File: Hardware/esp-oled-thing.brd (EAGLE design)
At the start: 48.3 x 27 mm, 44 parts, among them Q1 2.5A/30V, U1 MCP73831, U2 TPS61200

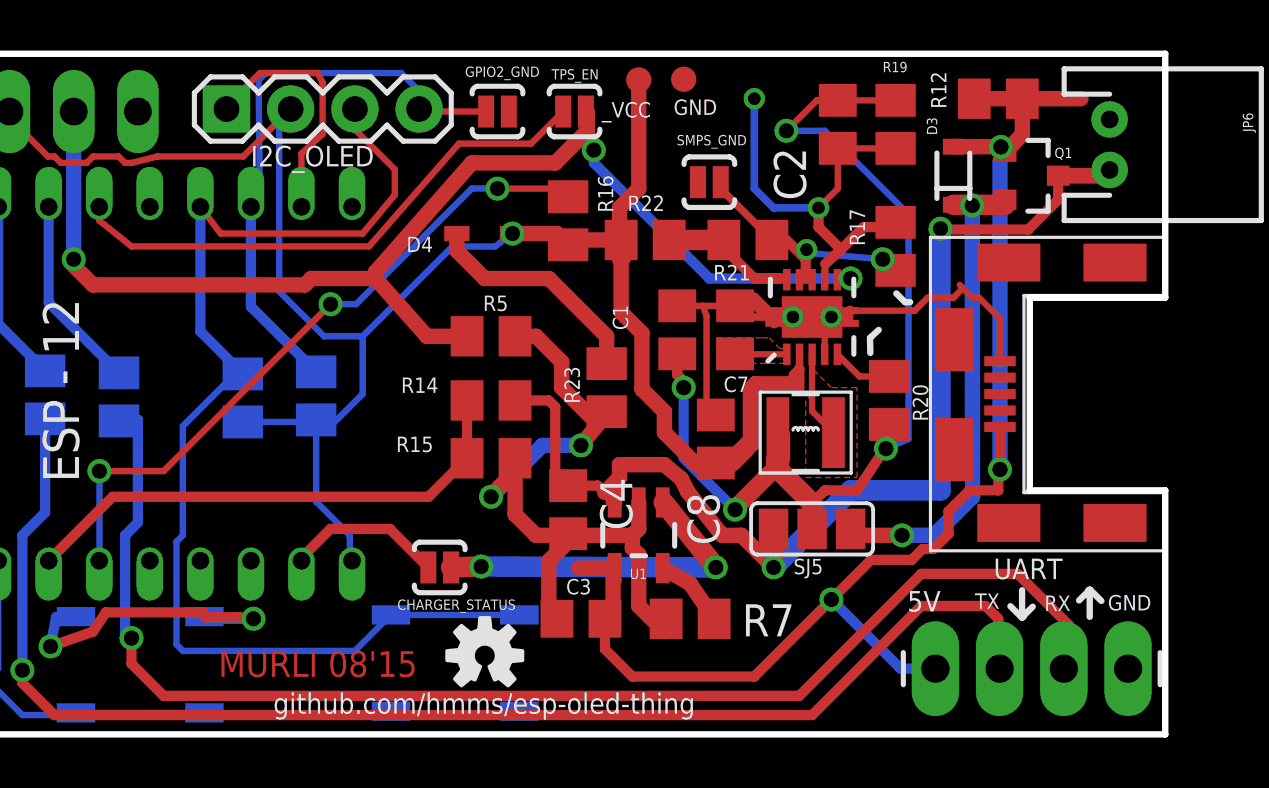
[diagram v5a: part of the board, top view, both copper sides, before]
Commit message: final DRC before sending it out. some errors fixed.
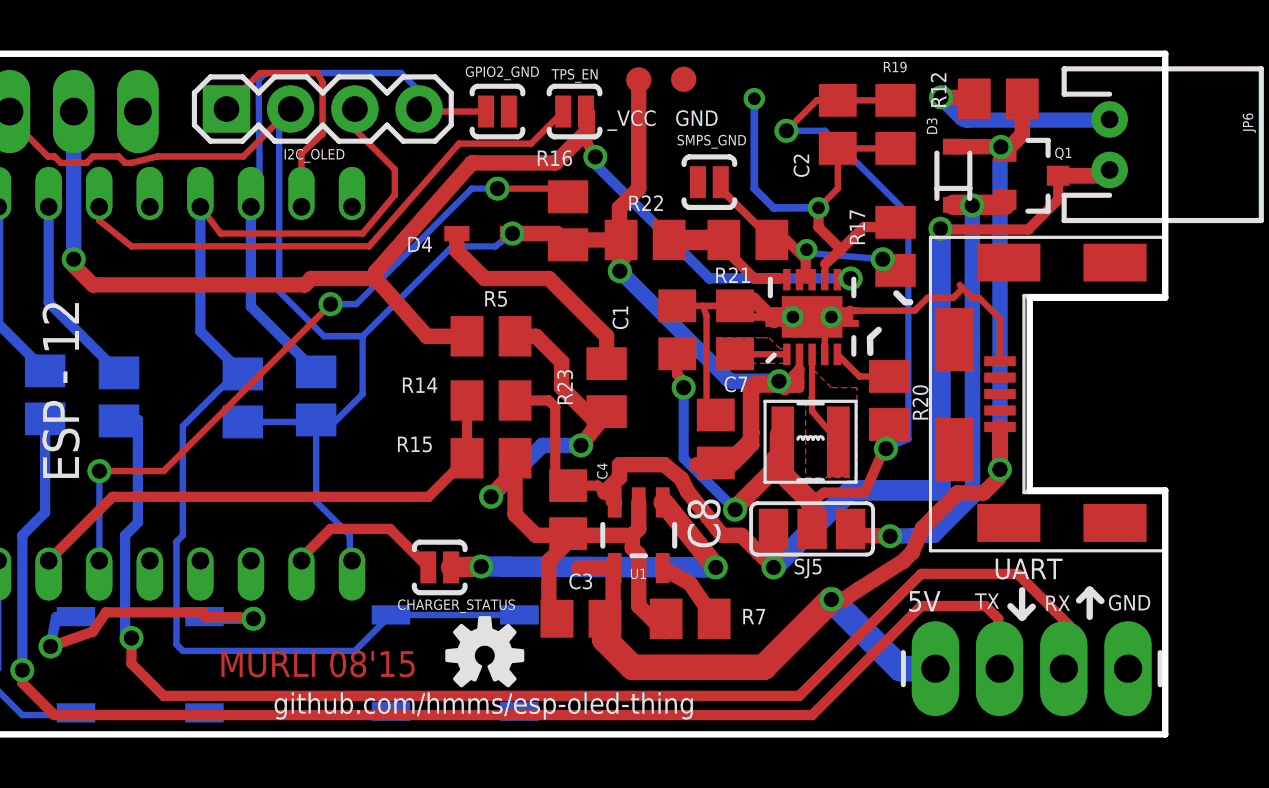
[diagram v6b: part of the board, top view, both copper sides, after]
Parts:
- moved U$3 0.41 mm to (34.2, 11.6)
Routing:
- net GND: track 81.8 -> 85.9 mm, vias 6 -> 7
- net 5VIN: track 49.7 -> 48.4 mm
- net VCC: track 85.7 -> 85.2 mm, vias 1 -> 3

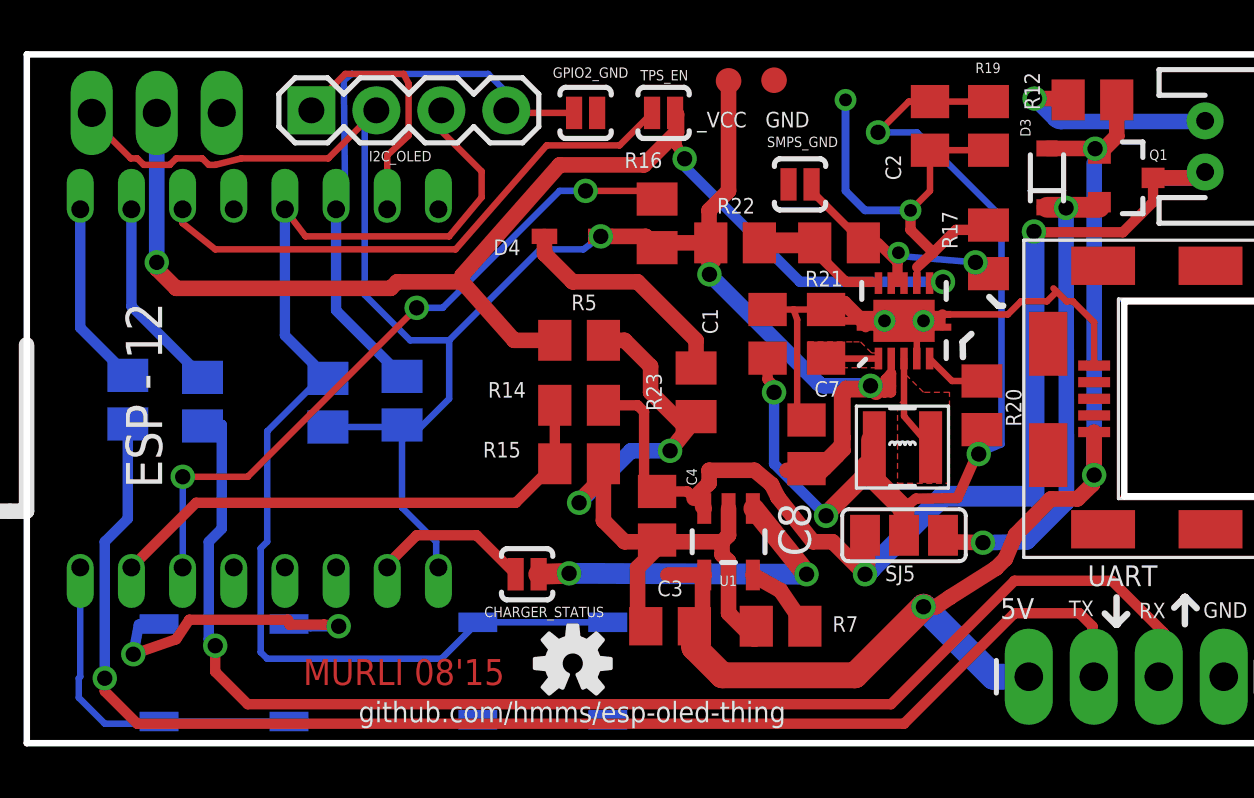
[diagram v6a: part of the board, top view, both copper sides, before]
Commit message: 'rev 2' hardware files sent to OSHPARK. NOT a final release, next release scheduled for end September with bug fixes - if any and aesthetic changes to fit in an enclosure.
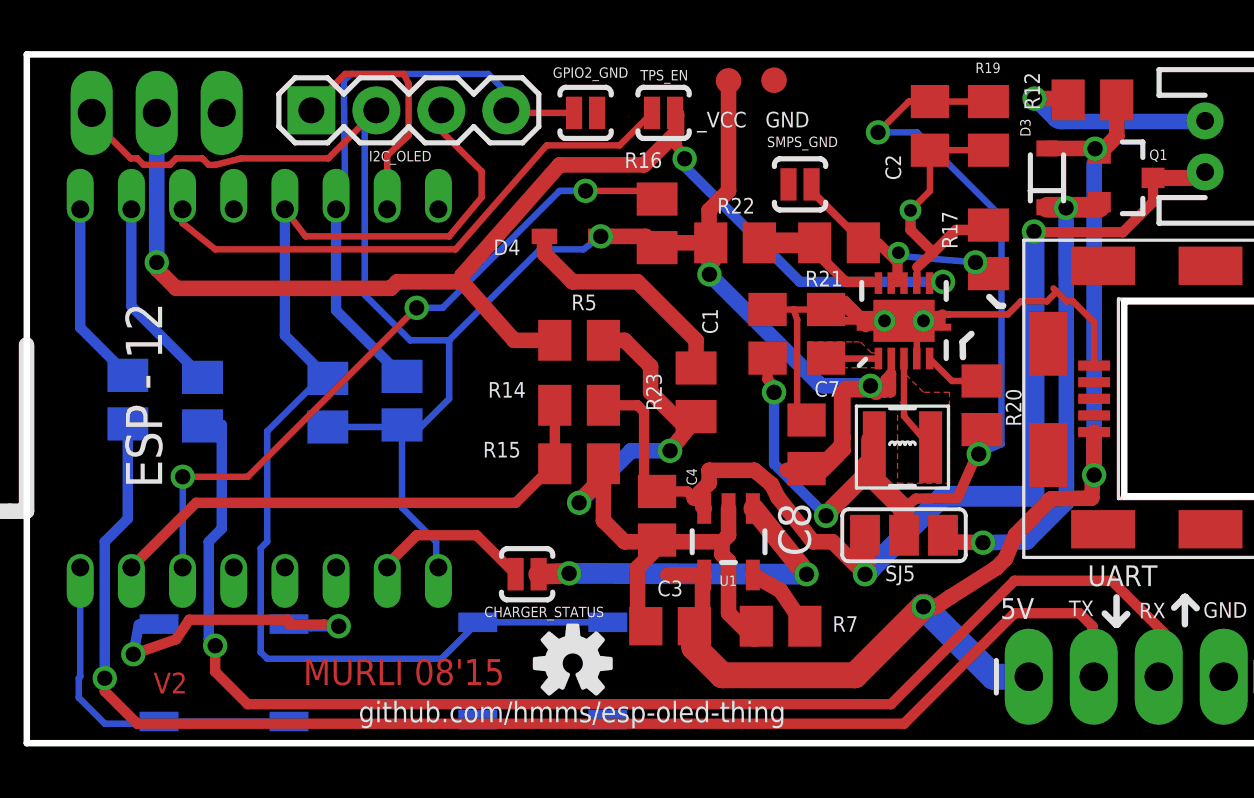
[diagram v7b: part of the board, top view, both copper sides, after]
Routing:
- net UVLO: track 17.5 -> 11.1 mm, vias 2 -> 1
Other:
- board text added: "V2"
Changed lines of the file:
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@@
 <wire x1="45.20945625" y1="5.6743625" x2="45.20945625" y2="5.65658125" width="0.254" layer="121"/>
 <wire x1="45.20945625" y1="5.65658125" x2="44.85131875" y2="5.29844375" width="0.254" layer="121"/>
+<text x="4.953" y="1.9431" size="0.8128" layer="1" font="vector">V2</text>
 </plain>
 <attributes>
@@
 </element>
 <element name="R1" library="adafruit" package="M0805" value="4.7K" x="11.77" y="13.31" locked="yes" smashed="yes" rot="MR270">
-<attribute name="NAME" x="10.474" y="16.654" size="1.27" layer="26" rot="MR180"/>
-<attribute name="VALUE" x="12.844" y="12.174" size="0.8128" layer="28" rot="MR90"/>
+<attribute name="NAME" x="10.36478125" y="10.9644" size="1.27" layer="26" rot="MR180"/>
+<attribute name="VALUE" x="11.043140625" y="15.630940625" size="0.8128" layer="28" rot="MR90"/>
 </element>
 <element name="R2" library="adafruit" package="M0805" value="4.7K" x="14.67" y="13.39" locked="yes" smashed="yes" rot="MR270">
-<attribute name="NAME" x="13.494" y="16.754" size="1.27" layer="26" rot="MR180"/>
-<attribute name="VALUE" x="16.856" y="14.506" size="0.8128" layer="28" rot="MR270"/>
+<attribute name="NAME" x="13.841978125" y="11.039" size="1.27" layer="26" rot="MR180"/>
+<attribute name="VALUE" x="13.5579625" y="15.51171875" size="0.8128" layer="28" rot="MR90"/>
 </element>
 <element name="U$2" library="esp8266modules" package="ESP12" value="ESP12" x="7.89" y="13.97" locked="yes" smashed="yes" rot="R90">
@@
 <element name="RST" library="SparkFun" package="TACTILE_SWITCH_SMD" value="" x="7.70968125" y="2.752859375" rot="MR0"/>
 <element name="R3" library="adafruit" package="M0805" value="100E" x="3.95" y="13.43" locked="yes" smashed="yes" rot="MR270">
-<attribute name="NAME" x="2.754" y="16.534" size="1.27" layer="26" rot="MR180"/>
-<attribute name="VALUE" x="2.936" y="14.646" size="0.8128" layer="28" rot="MR270"/>
+<attribute name="NAME" x="3.3059375" y="15.57338125" size="1.27" layer="26" rot="MR90"/>
+<attribute name="VALUE" x="2.76581875" y="14.463121875" size="0.8128" layer="28" rot="MR270"/>
 </element>
 <element name="R4" library="adafruit" package="M0805" value="100E" x="6.87" y="13.35" locked="yes" smashed="yes" rot="MR270">
-<attribute name="NAME" x="5.634" y="16.654" size="1.27" layer="26" rot="MR180"/>
-<attribute name="VALUE" x="5.856" y="14.566" size="0.8128" layer="28" rot="MR270"/>
+<attribute name="NAME" x="6.426978125" y="15.583178125" size="1.27" layer="26" rot="MR90"/>
+<attribute name="VALUE" x="9.191021875" y="14.733640625" size="0.8128" layer="28" rot="MR270"/>
 </element>
 <element name="I2C_OLED" library="SparkFun" package="1X04" value="" x="11.124" y="24.738" smashed="yes">
@@
 <wire x1="32.3723" y1="2.6543" x2="35.052" y2="5.334" width="1.016" layer="1"/>
 <wire x1="41.656" y1="10.414" x2="41.656" y2="10.11681875" width="0.6096" layer="1"/>
-<wire x1="41.656" y1="10.11681875" x2="41.0718" y2="9.5504" width="0.6096" layer="1"/>
-<wire x1="41.0718" y1="9.5504" x2="40.035478125" y2="9.5504" width="0.6096" layer="1"/>
+<wire x1="41.656" y1="10.11681875" x2="41.628059375" y2="9.58088125" width="0.6096" layer="1"/>
+<wire x1="41.628059375" y1="9.58088125" x2="40.035478125" y2="9.5504" width="0.6096" layer="1"/>
 <wire x1="41.722" y1="12.162" x2="41.722" y2="10.48" width="0.6096" layer="1"/>
 <wire x1="42.606" y1="23.728" x2="42.606" y2="25.146" width="0.6096" layer="1"/>
@@
 <wire x1="34.798" y1="18.034" x2="34.798" y2="17.993" width="0.254" layer="1"/>
 <wire x1="34.798" y1="17.993" x2="34.79" y2="17.985" width="0.254" layer="1"/>
-<via x="32.004" y="25.146" extent="1-16" drill="0.5"/>
-<wire x1="32.004" y1="21.59" x2="32.004" y2="25.146" width="0.3048" layer="16"/>
-<wire x1="32.004" y1="21.59" x2="32.766" y2="20.828" width="0.3048" layer="16"/>
-<wire x1="32.766" y1="20.828" x2="34.544" y2="20.828" width="0.3048" layer="16"/>
 <via x="34.544" y="20.828" extent="1-16" drill="0.5"/>
 <contactref element="C2" pad="2"/>

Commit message: parts ordered from Digikey,BOM added. Change quantity before ordering.
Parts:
- C1: value 10uF -> 10uF 10V
- C2, C7: value 0.1uF -> 0.1uF 10V
- C3, C4: value 4.7uF -> 4.7uF 10V
- C8: value 22uF -> 22uF 10V
- Q1: value 2.5A/30V -> DMP1045U
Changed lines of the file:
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@@
 <attribute name="VALUE" x="40.706040625" y="23.59151875" size="0.4064" layer="27" rot="R270"/>
 </element>
-<element name="Q1" library="SparkFun-DiscreteSemi" package="SOT23-3" value="2.5A/30V" x="42.926" y="22.098" smashed="yes" rot="R270">
+<element name="Q1" library="SparkFun-DiscreteSemi" package="SOT23-3" value="DMP1045U" x="42.926" y="22.098" smashed="yes" rot="R270">
 <attribute name="PROD_ID" value="TRANS-11308" x="50.546" y="34.798" size="1.778" layer="27" rot="R270" display="off"/>
 <attribute name="VALUE" value="2.5A/30V" x="50.546" y="34.798" size="1.778" layer="27" rot="R270" display="off"/>
@@
 <attribute name="VALUE" x="28.829" y="25.40761875" size="0.0254" layer="27"/>
 </element>
-<element name="C1" library="rcl" package="C0805" value="10uF" x="28.956" y="16.002" smashed="yes" rot="R90">
+<element name="C1" library="rcl" package="C0805" value="10uF 10V" x="28.956" y="16.002" smashed="yes" rot="R90">
 <attribute name="NAME" x="27.01544375" y="15.9893" size="0.6096" layer="25" rot="R90"/>
 <attribute name="VALUE" x="27.26435625" y="17.274534375" size="0.6096" layer="27" rot="R270"/>
 </element>
-<element name="C2" library="rcl" package="C0805" value="0.1uF" x="35.306" y="24.13" smashed="yes" rot="R270">
+<element name="C2" library="rcl" package="C0805" value="0.1uF 10V" x="35.306" y="24.13" smashed="yes" rot="R270">
 <attribute name="NAME" x="33.5661" y="23.0124" size="0.6096" layer="25" rot="R270"/>
 <attribute name="VALUE" x="36.357559375" y="22.0218" size="0.6096" layer="27" rot="R180"/>
 </element>
-<element name="C7" library="rcl" package="C0805" value="0.1uF" x="31.242" y="16.002" smashed="yes" rot="R90">
+<element name="C7" library="rcl" package="C0805" value="0.1uF 10V" x="31.242" y="16.002" smashed="yes" rot="R90">
 <attribute name="NAME" x="31.790640625" y="14.152878125" size="0.6096" layer="25" rot="R180"/>
 <attribute name="VALUE" x="30.28695625" y="15.483840625" size="0.4064" layer="27" rot="R90"/>
 </element>
-<element name="C8" library="rcl" package="C0805" value="22uF" x="30.48" y="11.684" smashed="yes" rot="R90">
+<element name="C8" library="rcl" package="C0805" value="22uF 10V" x="30.48" y="11.684" smashed="yes" rot="R90">
 <attribute name="NAME" x="30.65018125" y="7.30758125" size="1.27" layer="25" rot="R90"/>
 <attribute name="VALUE" x="32.115759375" y="10.767059375" size="0.6096" layer="27" rot="R90"/>
@@
 <attribute name="VALUE" x="29.16428125" y="2.8473375" size="0.6096" layer="27"/>
 </element>
-<element name="C3" library="rcl" package="C0805" value="4.7uF" x="25.146" y="4.572" smashed="yes" rot="R180">
+<element name="C3" library="rcl" package="C0805" value="4.7uF 10V" x="25.146" y="4.572" smashed="yes" rot="R180">
 <attribute name="NAME" x="25.648915625" y="6.355078125" size="0.6096" layer="25" rot="R180"/>
 <attribute name="VALUE" x="26.2763" y="3.44931875" size="0.6096" layer="27" rot="R180"/>
 </element>
-<element name="C4" library="rcl" package="C0805" value="4.7uF" x="24.638" y="8.89" smashed="yes" rot="R270">
+<element name="C4" library="rcl" package="C0805" value="4.7uF 10V" x="24.638" y="8.89" smashed="yes" rot="R270">
 <attribute name="NAME" x="25.78861875" y="10.74928125" size="0.4064" layer="25" rot="R270"/>
 <attribute name="VALUE" x="22.9616" y="9.5504" size="0.6096" layer="27" rot="R270"/>
@@
 </signal>
 </signals>
-<errors>
-</errors>
 </board>
 </drawing>
